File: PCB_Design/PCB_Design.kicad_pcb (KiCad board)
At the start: 2 copper layers, 54 parts, among them IC1 MIC37303YME, J1 TP4056, J2 632723300011, SW1 SW_Push, SW2 SW_Push, U1 ESP32-WROOM-32

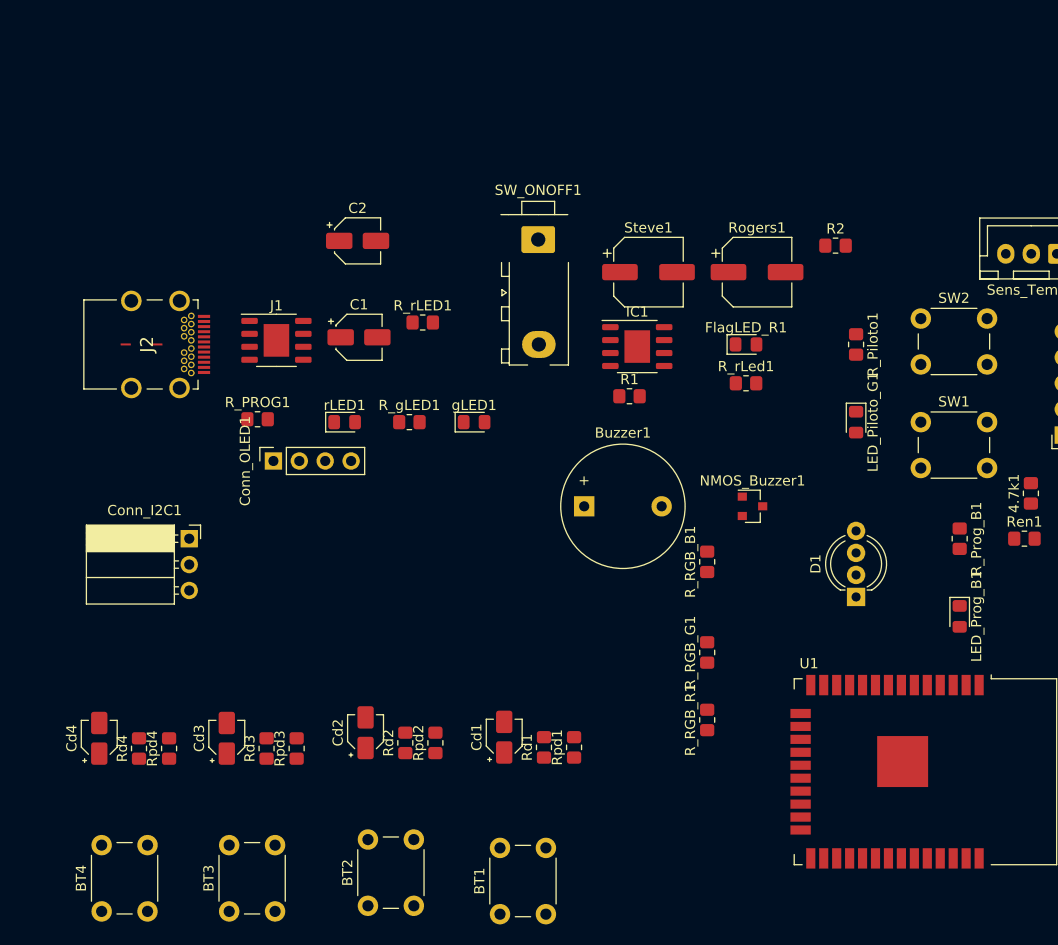
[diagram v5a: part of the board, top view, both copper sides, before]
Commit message: Nuevas huellas y un poco más de orden
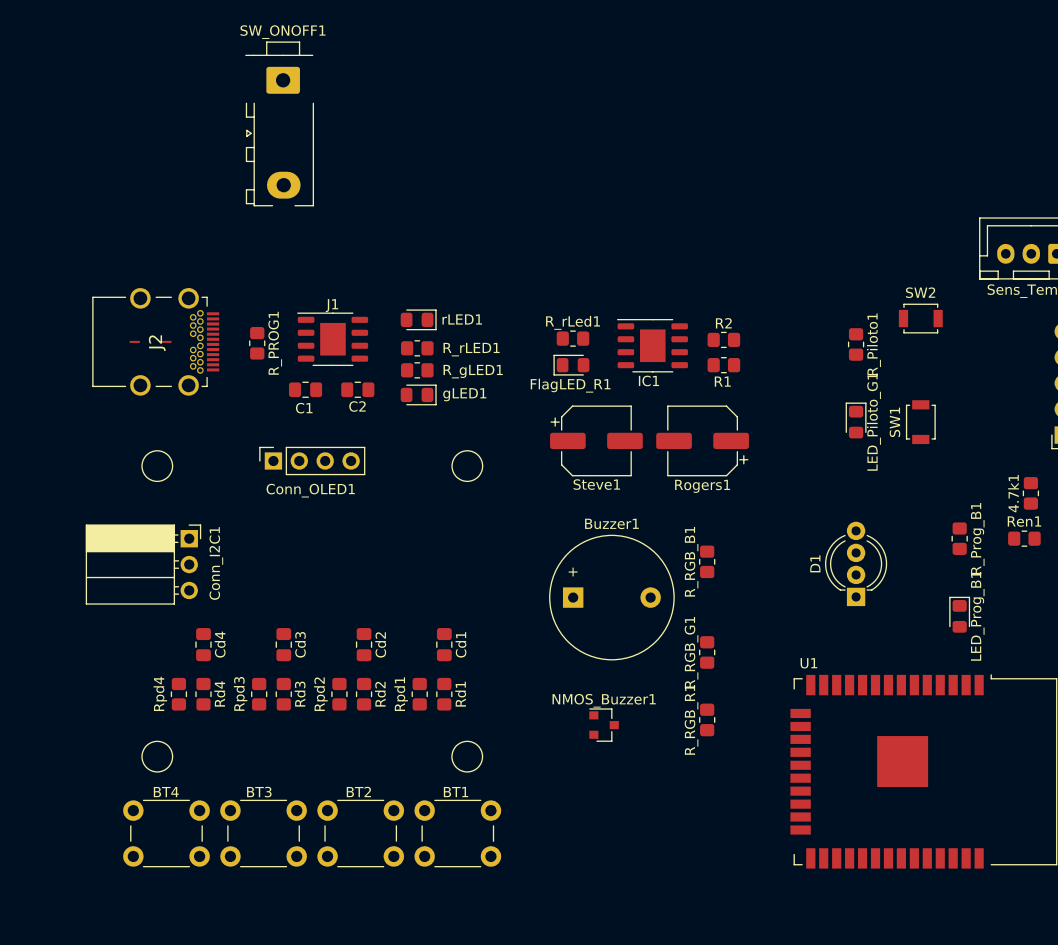
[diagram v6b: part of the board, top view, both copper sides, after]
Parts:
- C1, C2: footprint Capacitor_SMD:CP_Elec_4x5.8 -> Capacitor_SMD:C_0805_2012Metric_Pad1.18x1.45mm_HandSolder
- Cd1, Cd2, Cd3, Cd4: footprint Capacitor_SMD:CP_Elec_3x5.4 -> Capacitor_SMD:C_0805_2012Metric_Pad1.18x1.45mm_HandSolder
- SW1, SW2: footprint Button_Switch_THT:SW_PUSH_6mm_H5mm -> Button_Switch_SMD:SW_SPST_B3U-1000P
- moved SW_ONOFF1 29.5 mm to (83.6, 78.4)
- moved NMOS_Buzzer1 25.9 mm to (115.0, 136.4)
- moved R_rLed1 17.5 mm to (111.9, 98.5)
- moved Rogers1 17.4 mm to (124.6, 108.5), turned to 180 degrees
- moved Steve1 17.3 mm to (114.2, 108.5)
- moved FlagLED_R1 17.1 mm to (111.9, 101.1)
- moved Rpd1 16.0 mm to (96.9, 133.4)
- moved C2 14.6 mm to (90.8, 103.5), turned to 180 degrees
- moved R2 14.3 mm to (126.7, 98.6)
- moved Cd4 13.7 mm to (75.7, 128.5), turned to 270 degrees
- moved rLED1 12.3 mm to (96.6, 96.6), turned to 180 degrees
- moved Rd1 11.1 mm to (99.3, 133.4), turned to 270 degrees
- moved BT4 11.0 mm to (75.3, 149.3), turned to 180 degrees
- moved Cd1 10.8 mm to (99.3, 128.5), turned to 270 degrees
- moved Cd3 10.8 mm to (83.6, 128.5), turned to 270 degrees
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
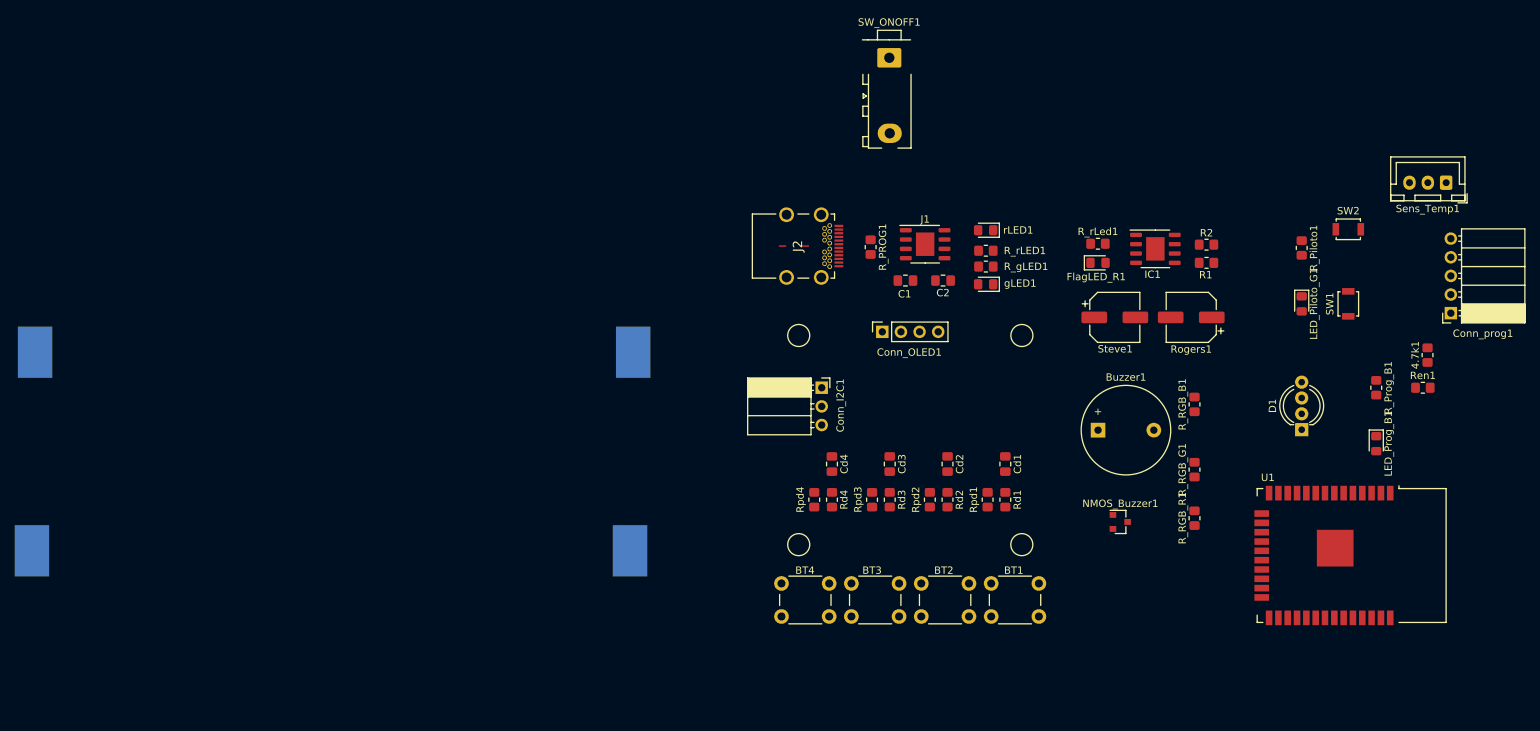
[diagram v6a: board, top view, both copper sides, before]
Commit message: Nuevas huellas y un poco más de orden
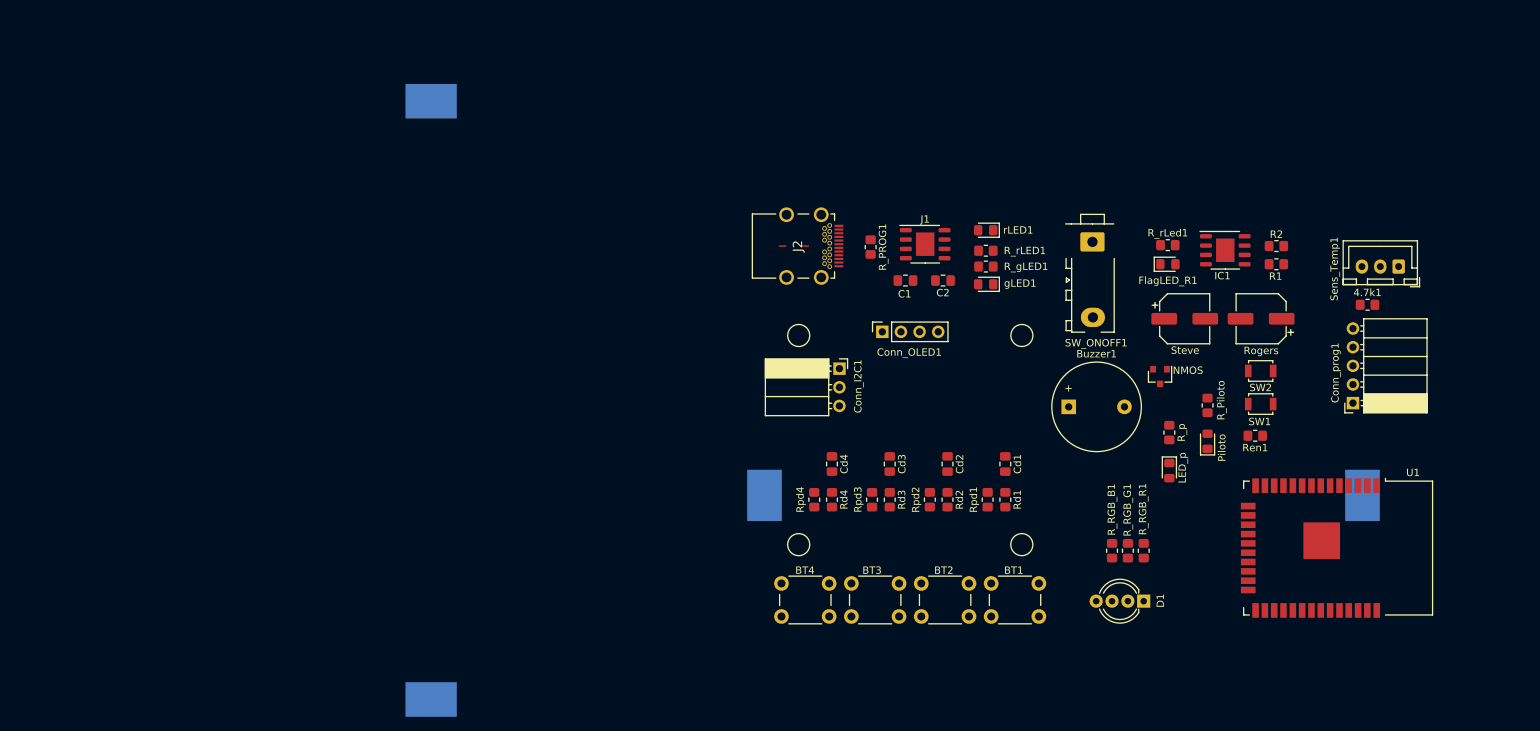
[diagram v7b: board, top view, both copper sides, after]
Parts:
- removed LED_Piloto_G1, LED_Prog_B1: LED, LED_SMD:LED_0805_2012Metric_Pad1.15x1.40mm_HandSolder
- removed NMOS_Buzzer1: Q_NMOS_GSD, Package_TO_SOT_SMD:SOT-23
- removed R_Piloto1: 180, Resistor_SMD:R_0805_2012Metric_Pad1.20x1.40mm_HandSolder
- removed R_Prog_B1: 47, Resistor_SMD:R_0805_2012Metric_Pad1.20x1.40mm_HandSolder
- removed Rogers1, Steve1: 47u, Capacitor_SMD:CP_Elec_6.3x5.9
- added LED_p: LED, LED_SMD:LED_0805_2012Metric_Pad1.15x1.40mm_HandSolder, F.Cu at (121.7, 129.4)
- added NMOS: Q_NMOS_GSD, Package_TO_SOT_SMD:SOT-23, F.Cu at (120.4, 116.6)
- added Piloto: LED, LED_SMD:LED_0805_2012Metric_Pad1.15x1.40mm_HandSolder, F.Cu at (126.9, 125.4)
- added R_Piloto: 180, Resistor_SMD:R_0805_2012Metric_Pad1.20x1.40mm_HandSolder, F.Cu at (126.9, 120.5)
- added R_p: 47, Resistor_SMD:R_0805_2012Metric_Pad1.20x1.40mm_HandSolder, F.Cu at (121.7, 124.2)
- added Rogers: 47u, Capacitor_SMD:CP_Elec_6.3x5.9, F.Cu at (134.2, 108.7)
- added Steve: 47u, Capacitor_SMD:CP_Elec_6.3x5.9, F.Cu at (123.8, 108.7)
- moved Battery1 100.1 mm to (71.2, 132.8)
- moved Battery2 65.1 mm to (21.1, 155.8), turned to 90 degrees
- moved SW_ONOFF1 37.4 mm to (111.3, 103.4)
- moved D1 31.8 mm to (118.2, 147.2), turned to 180 degrees
- moved Ren1 23.8 mm to (133.4, 124.7), turned to 180 degrees
- moved R_RGB_B1 22.9 mm to (113.9, 140.3)
- moved SW2 22.7 mm to (134.1, 115.8)
- moved SW1 18.1 mm to (134.1, 120.3), turned to 180 degrees
- moved Conn_prog1 18.1 mm to (146.7, 120.2)
- moved R_RGB_G1 14.3 mm to (116.0, 140.3)
- moved Sens_Temp1 13.1 mm to (152.9, 101.6)
- moved 4.7k1 10.7 mm to (148.7, 106.8), turned to 0 degrees
- moved IC1 9.53 mm to (129.3, 99.4)
- moved R_rLed1 9.53 mm to (121.5, 98.7)
- moved FlagLED_R1 9.53 mm to (121.5, 101.3)
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
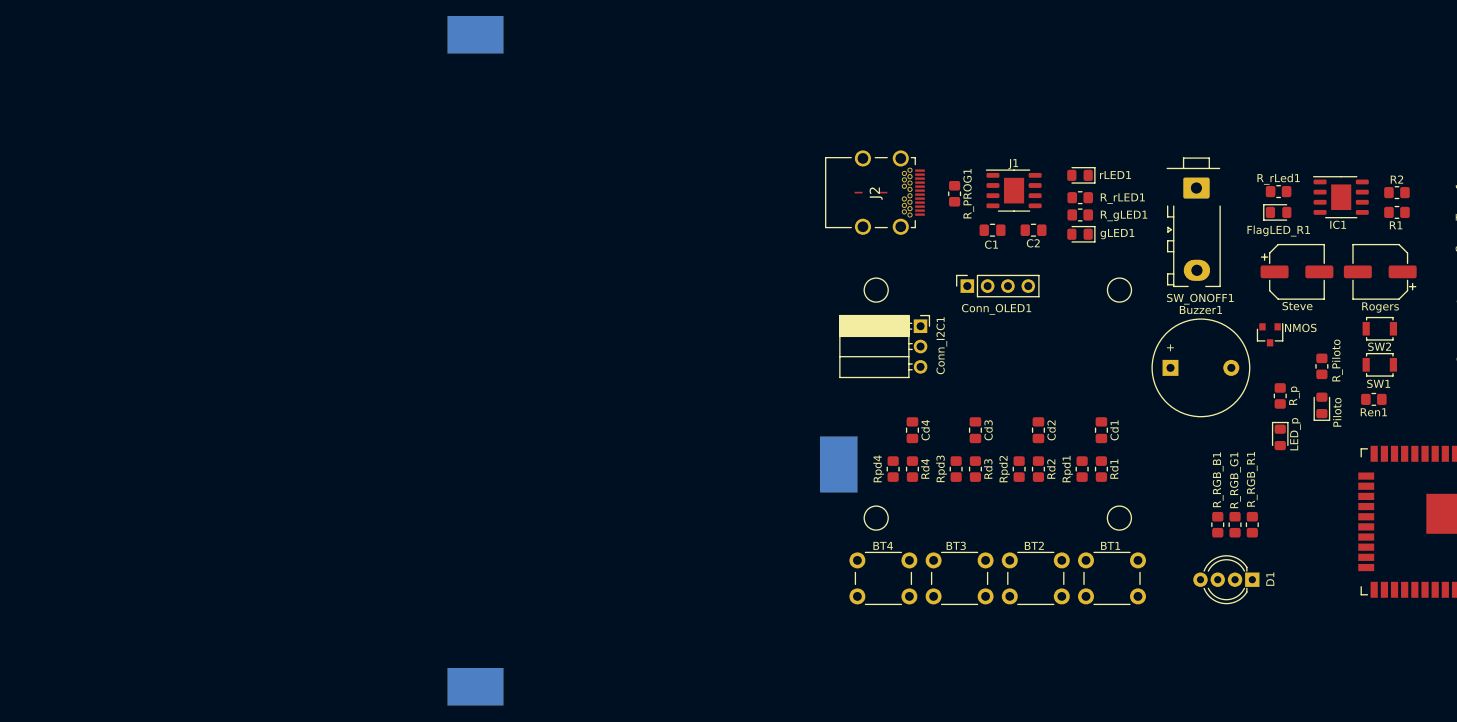
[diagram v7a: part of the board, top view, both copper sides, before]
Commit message: Nuevas huellas y un poco más de orden
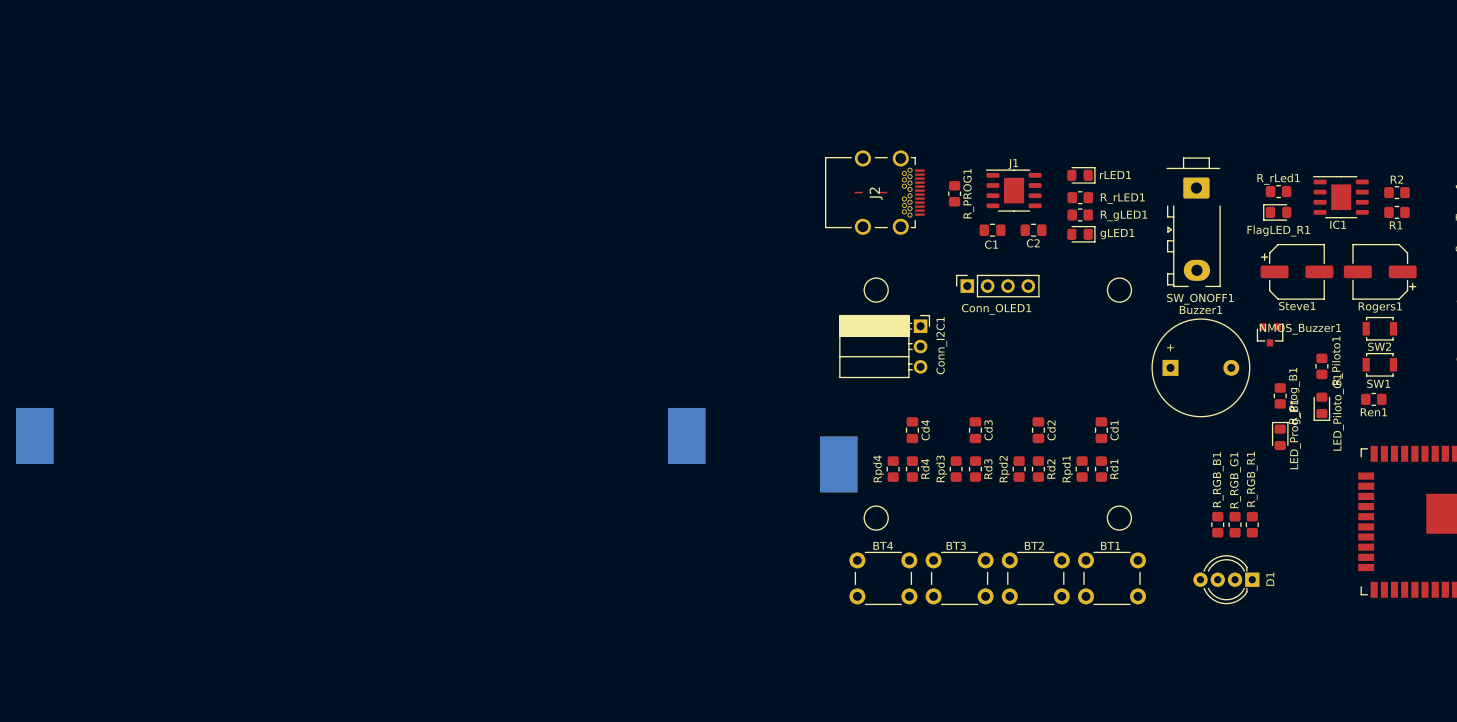
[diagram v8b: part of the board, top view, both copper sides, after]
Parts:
- moved Battery2 34.3 mm to (42.7, 129.2), turned to 180 degrees
- renumbered Piloto to LED_Piloto_G1, LED_p to LED_Prog_B1, NMOS to NMOS_Buzzer1, R_Piloto to R_Piloto1, R_p to R_Prog_B1, Rogers to Rogers1, Steve to Steve1
